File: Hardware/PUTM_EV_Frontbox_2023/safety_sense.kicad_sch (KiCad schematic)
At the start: 18 parts, among them U10 TLP291-4, U11 TLP291-4

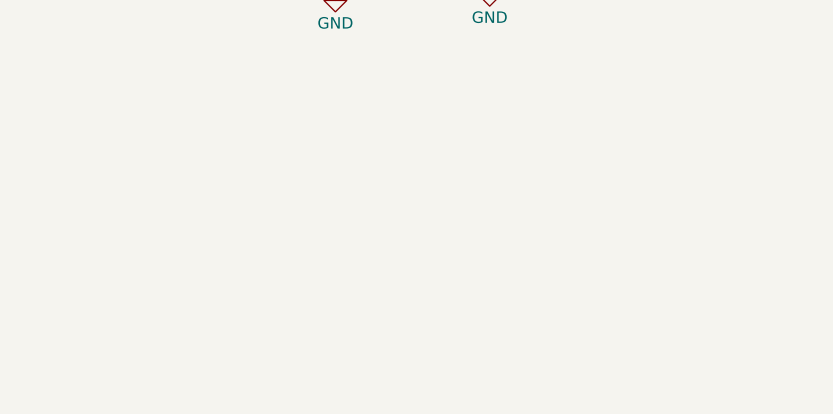
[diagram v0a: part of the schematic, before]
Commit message: Moved sw cap closer to pins
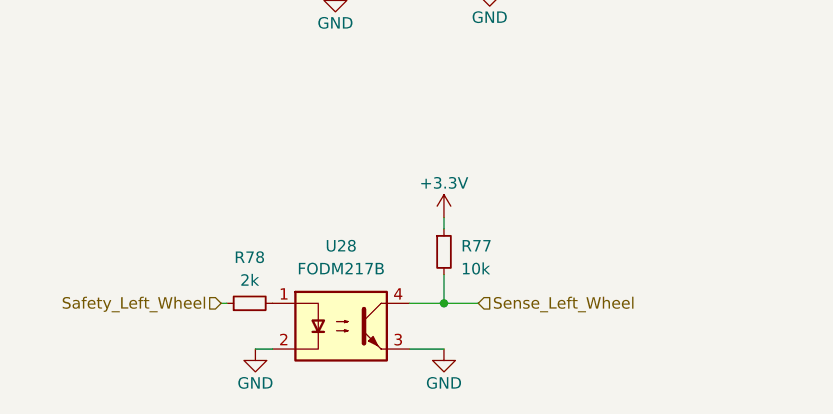
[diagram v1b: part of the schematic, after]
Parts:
- added R77: 10k, Resistor_SMD:R_0402_1005Metric, symbol Device:R_Small
- added R78: 2k, Resistor_SMD:R_0402_1005Metric, symbol Device:R_Small
- added U28: FODM217B, Package_SO:SOP-4_4.4x2.6mm_P1.27mm, symbol Isolator:FODM217B
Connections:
- net +3.3V: now also R77.1
- net GND: now also U28.2, U28.3
- new net: R78.2, U28.1
- new net Safety_Left_Wheel: R78.1
- new net Sense_Left_Wheel: R77.2, U28.4
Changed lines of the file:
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@@
   (junction (at 127 134.62) (diameter 0) (color 0 0 0 0)
   )
+  (junction (at 121.285 175.895) (diameter 0) (color 0 0 0 0)
+  )
   (wire (pts (xy 125.73 107.95) (xy 127 107.95))
     (stroke (width 0) (type default))
@@
     (stroke (width 0) (type default))
   )
+  (wire (pts (xy 100.33 180.975) (xy 102.235 180.975))
+    (stroke (width 0) (type default))
+  )
   (wire (pts (xy 194.31 74.295) (xy 194.31 75.565))
     (stroke (width 0) (type default))
@@
     (stroke (width 0) (type default))
   )
+  (wire (pts (xy 121.285 175.895) (xy 121.285 172.72))
+    (stroke (width 0) (type default))
+  )
   (wire (pts (xy 108.585 62.23) (xy 109.855 62.23))
     (stroke (width 0) (type default))
@@
     (stroke (width 0) (type default))
   )
+  (wire (pts (xy 121.285 166.37) (xy 121.285 167.64))
+    (stroke (width 0) (type default))
+  )
   (wire (pts (xy 176.53 88.9) (xy 176.53 87.63))
     (stroke (width 0) (type default))
   )
+  (wire (pts (xy 96.52 175.895) (xy 97.155 175.895))
+    (stroke (width 0) (type default))
+  )
   (wire (pts (xy 126.365 57.15) (xy 128.27 57.15))
     (stroke (width 0) (type default))
@@
     (stroke (width 0) (type default))
   )
+  (wire (pts (xy 121.285 175.895) (xy 125.095 175.895))
+    (stroke (width 0) (type default))
+  )
   (wire (pts (xy 108.585 134.62) (xy 110.49 134.62))
     (stroke (width 0) (type default))
@@
   )
   (wire (pts (xy 193.04 82.55) (xy 194.31 82.55))
+    (stroke (width 0) (type default))
+  )
+  (wire (pts (xy 121.285 180.975) (xy 117.475 180.975))
+    (stroke (width 0) (type default))
+  )
+  (wire (pts (xy 121.285 175.895) (xy 117.475 175.895))
     (stroke (width 0) (type default))
   )
@@
     (effects (font (size 1.27 1.27)) (justify left))
   )
+  (hierarchical_label "Safety_Left_Wheel" (shape input) (at 96.52 175.895 180) (fields_autoplaced)
+    (effects (font (size 1.27 1.27)) (justify right))
+  )
   (hierarchical_label "Sense_right_kill" (shape output) (at 128.905 82.55 0) (fields_autoplaced)
     (effects (font (size 1.27 1.27)) (justify left))
@@
   )
   (hierarchical_label "Sense_left_kill" (shape output) (at 196.215 82.55 0) (fields_autoplaced)
+    (effects (font (size 1.27 1.27)) (justify left))
+  )
+  (hierarchical_label "Sense_Left_Wheel" (shape input) (at 125.095 175.895 0) (fields_autoplaced)
     (effects (font (size 1.27 1.27)) (justify left))
   )
@@
     )
   )
+  (symbol (lib_id "Device:R_Small") (at 99.695 175.895 90) (unit 1)
+    (in_bom yes) (on_board yes) (dnp no) (fields_autoplaced)
+    (property "Reference" "R78" (at 99.695 170.815 90)
+      (effects (font (size 1.27 1.27)))
+    )
+    (property "Value" "2k" (at 99.695 173.355 90)
+      (effects (font (size 1.27 1.27)))
+    )
+    (property "Footprint" "Resistor_SMD:R_0402_1005Metric" (at 99.695 175.895 0)
+      (effects (font (size 1.27 1.27)) hide)
+    )
+    (property "Datasheet" "~" (at 99.695 175.895 0)
+      (effects (font (size 1.27 1.27)) hide)
+    )
+    (pin "1")
+    (pin "2")
+    (instances
+      (project "PUTM_EV_Frontbox_2023"
+        (path "/b652b05a-4e3d-4ad1-b032-18886abe7d45/d8521410-c497-472e-ae31-9f909ba7779b"
+          (reference "R78") (unit 1)
+        )
+      )
+    )
+  )
   (symbol (lib_id "power:GND") (at 194.945 113.665 0) (unit 1)
     (in_bom yes) (on_board yes) (dnp no)
@@
         (path "/b652b05a-4e3d-4ad1-b032-18886abe7d45/d8521410-c497-472e-ae31-9f909ba7779b"
           (reference "R12") (unit 1)
+        )
+      )
+    )
+  )
+  (symbol (lib_id "Device:R_Small") (at 121.285 170.18 0) (unit 1)
+    (in_bom yes) (on_board yes) (dnp no) (fields_autoplaced)
+    (property "Reference" "R77" (at 123.19 169.545 0)
+      (effects (font (size 1.27 1.27)) (justify left))
+    )
+    (property "Value" "10k" (at 123.19 172.085 0)
+      (effects (font (size 1.27 1.27)) (justify left))
+    )
+    (property "Footprint" "Resistor_SMD:R_0402_1005Metric" (at 121.285 170.18 0)
+      (effects (font (size 1.27 1.27)) hide)
+    )
+    (property "Datasheet" "~" (at 121.285 170.18 0)
+      (effects (font (size 1.27 1.27)) hide)
+    )
+    (pin "1")
+    (pin "2")
+    (instances
+      (project "PUTM_EV_Frontbox_2023"
+        (path "/b652b05a-4e3d-4ad1-b032-18886abe7d45/d8521410-c497-472e-ae31-9f909ba7779b"
+          (reference "R77") (unit 1)
         )
       )
@@
     )
   )
+  (symbol (lib_id "power:GND") (at 100.33 180.975 0) (unit 1)
+    (in_bom yes) (on_board yes) (dnp no)
+    (property "Reference" "#PWR0135" (at 100.33 187.325 0)
+      (effects (font (size 1.27 1.27)) hide)
+    )
+    (property "Value" "GND" (at 100.33 184.785 0)
+      (effects (font (size 1.27 1.27)))
+    )
+    (property "Footprint" "" (at 100.33 180.975 0)
+      (effects (font (size 1.27 1.27)) hide)
+    )
+    (property "Datasheet" "" (at 100.33 180.975 0)
+      (effects (font (size 1.27 1.27)) hide)
+    )
+    (pin "1")
+    (instances
+      (project "PUTM_EV_Frontbox_2023"
+        (path "/b652b05a-4e3d-4ad1-b032-18886abe7d45/d8521410-c497-472e-ae31-9f909ba7779b"
+          (reference "#PWR0135") (unit 1)
+        )
+      )
+    )
+  )
+  (symbol (lib_id "power:GND") (at 121.285 180.975 0) (unit 1)
+    (in_bom yes) (on_board yes) (dnp no)
+    (property "Reference" "#PWR0134" (at 121.285 187.325 0)
+      (effects (font (size 1.27 1.27)) hide)
+    )
+    (property "Value" "GND" (at 121.285 184.785 0)
+      (effects (font (size 1.27 1.27)))
+    )
+    (property "Footprint" "" (at 121.285 180.975 0)
+      (effects (font (size 1.27 1.27)) hide)
+    )
+    (property "Datasheet" "" (at 121.285 180.975 0)
+      (effects (font (size 1.27 1.27)) hide)
+    )
+    (pin "1")
+    (instances
+      (project "PUTM_EV_Frontbox_2023"
+        (path "/b652b05a-4e3d-4ad1-b032-18886abe7d45/d8521410-c497-472e-ae31-9f909ba7779b"
+          (reference "#PWR0134") (unit 1)
+        )
+      )
+    )
+  )
   (symbol (lib_id "Isolator:TLP291-4") (at 186.69 110.49 0) (unit 3)
     (in_bom yes) (on_board yes) (dnp no) (fields_autoplaced)
@@
     )
   )
+  (symbol (lib_id "power:+3.3V") (at 121.285 166.37 0) (unit 1)
+    (in_bom yes) (on_board yes) (dnp no) (fields_autoplaced)
+    (property "Reference" "#PWR0120" (at 121.285 170.18 0)
+      (effects (font (size 1.27 1.27)) hide)
+    )
+    (property "Value" "+3.3V" (at 121.285 162.56 0)
+      (effects (font (size 1.27 1.27)))
+    )
+    (property "Footprint" "" (at 121.285 166.37 0)
+      (effects (font (size 1.27 1.27)) hide)
+    )
+    (property "Datasheet" "" (at 121.285 166.37 0)
+      (effects (font (size 1.27 1.27)) hide)
+    )
+    (pin "1")
+    (instances
+      (project "PUTM_EV_Frontbox_2023"
+        (path "/b652b05a-4e3d-4ad1-b032-18886abe7d45/d8521410-c497-472e-ae31-9f909ba7779b"
+          (reference "#PWR0120") (unit 1)
+        )
+      )
+    )
+  )
   (symbol (lib_id "Device:R_Small") (at 106.045 107.95 90) (unit 1)
     (in_bom yes) (on_board yes) (dnp no) (fields_autoplaced)
@@
         )
       )
+    )
+  )
+  (symbol (lib_id "Isolator:FODM217B") (at 109.855 178.435 0) (unit 1)
+    (in_bom yes) (on_board yes) (dnp no) (fields_autoplaced)
+    (property "Reference" "U28" (at 109.855 169.545 0)
+      (effects (font (size 1.27 1.27)))
+    )
+    (property "Value" "FODM217B" (at 109.855 172.085 0)
+      (effects (font (size 1.27 1.27)))
+    )
+    (property "Footprint" "Package_SO:SOP-4_4.4x2.6mm_P1.27mm" (at 109.855 183.515 0)
+      (effects (font (size 1.27 1.27) italic) hide)
+    )
+    (property "Datasheet" "https://www.onsemi.com/pub/Collateral/FODM214-D.PDF" (at 109.855 178.435 0)
+      (effects (font (size 1.27 1.27)) (justify left) hide)
+    )
+    (pin "1")
+    (pin "2")
+    (pin "3")
+    (pin "4")
+    (instances
+      (project "PUTM_EV_Frontbox_2023"
+        (path "/b652b05a-4e3d-4ad1-b032-18886abe7d45/d8521410-c497-472e-ae31-9f909ba7779b"
+          (reference "U28") (unit 1)
+        )
+      )

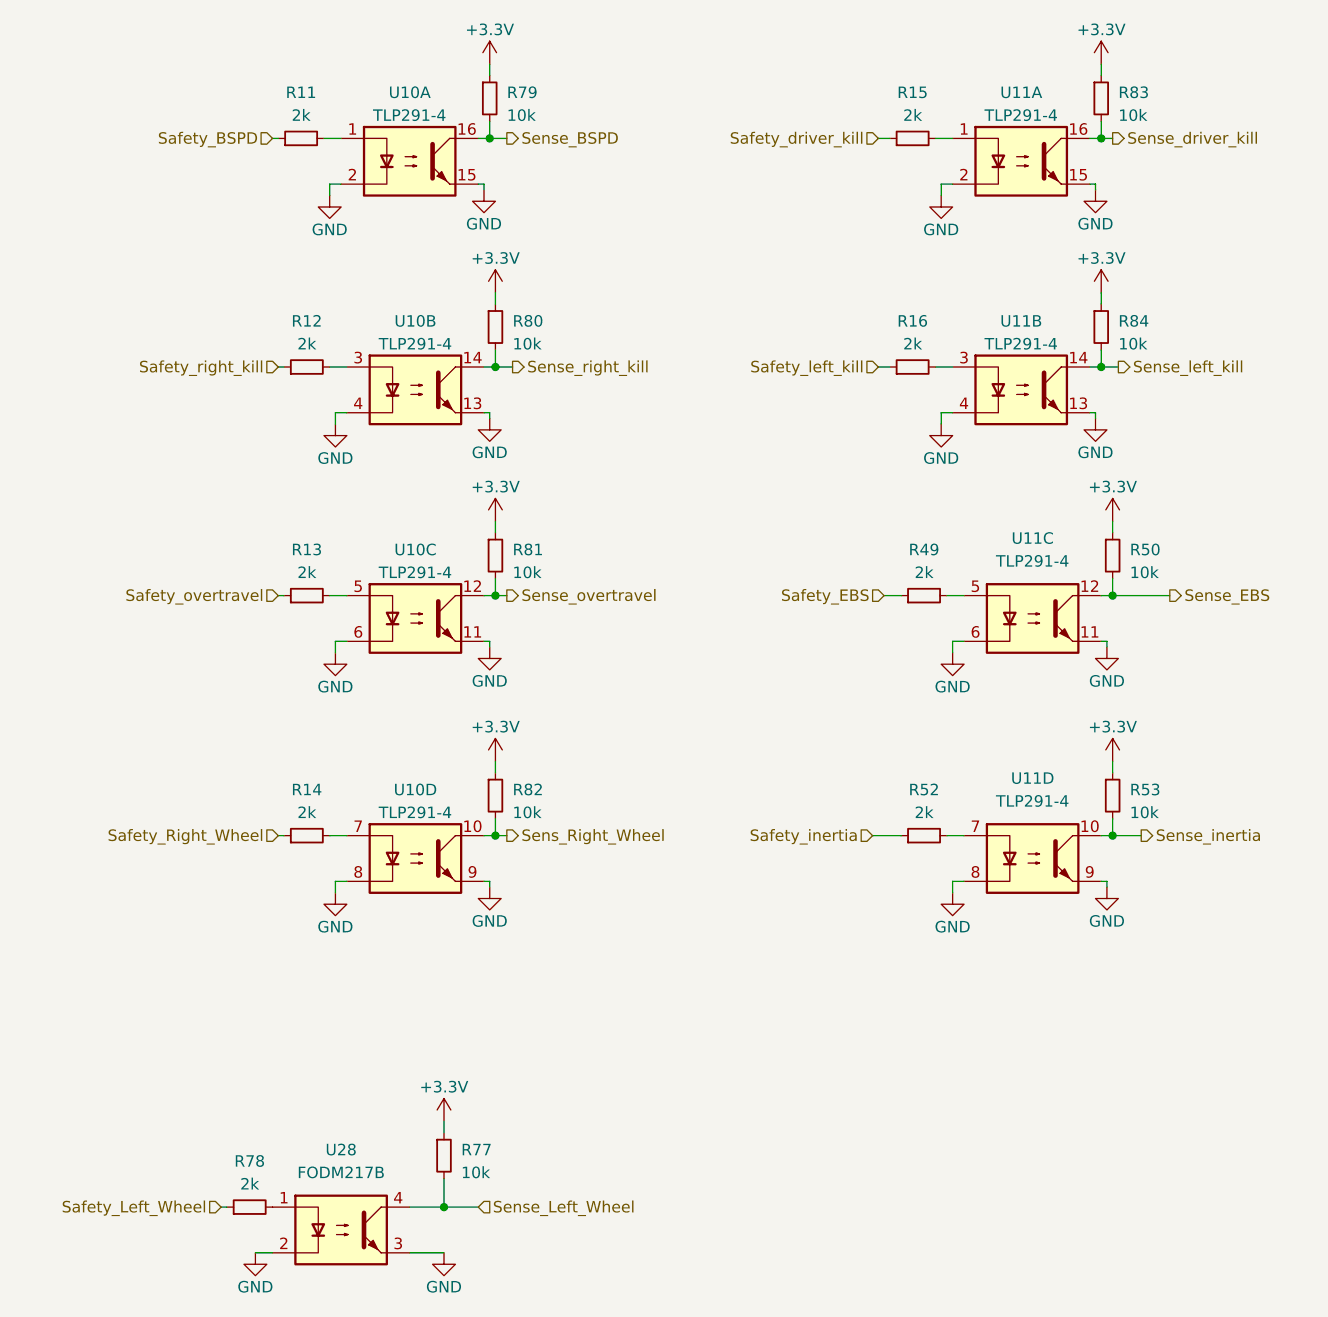
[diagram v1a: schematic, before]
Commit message: Added gearbox temperature sensors on schematic
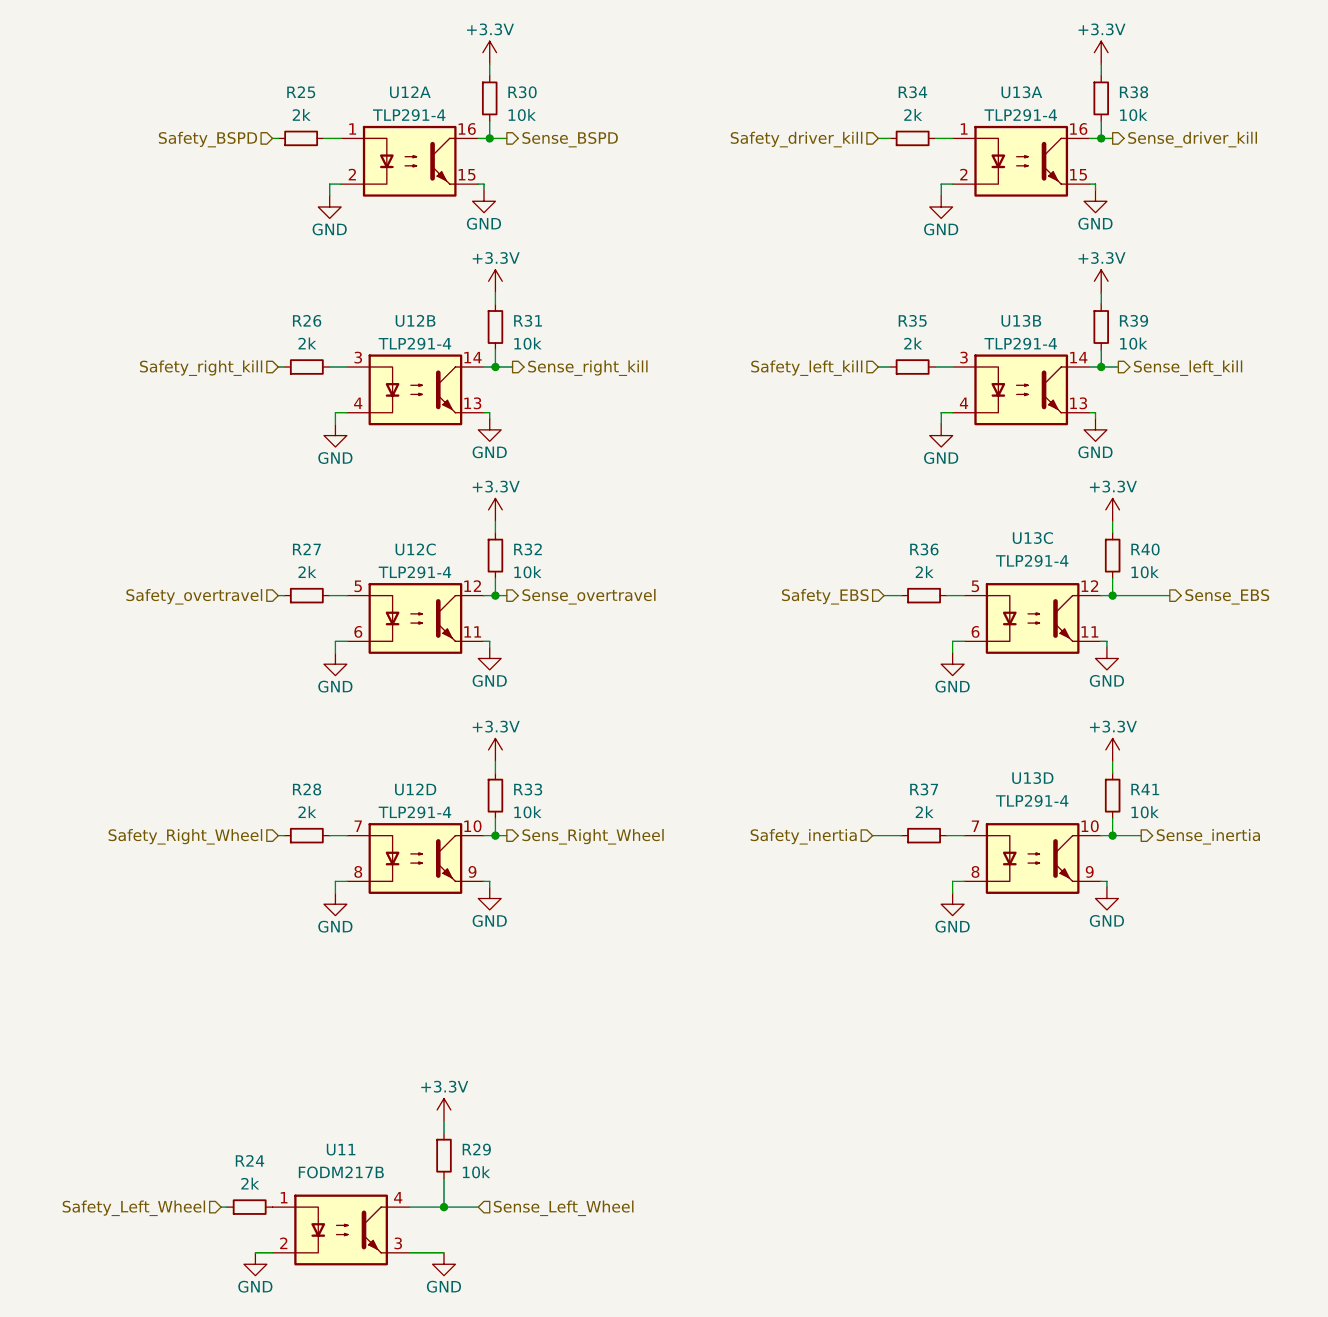
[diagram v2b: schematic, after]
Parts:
- renumbered R78 to R24, R11 to R25, R12 to R26, R13 to R27, R14 to R28, R77 to R29, R79 to R30, R80 to R31, R81 to R32, R82 to R33, R15 to R34, R16 to R35, R49 to R36, R52 to R37, R83 to R38, R84 to R39, R50 to R40, R53 to R41, U28 to U11, U10 to U12, U11 to U13
